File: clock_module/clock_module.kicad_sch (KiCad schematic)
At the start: 19 parts, among them SW1 SW_SPST, SW2 SW_Push, SW3 SW_SPDT, SW4 SW_SPDT, U1 74HC14

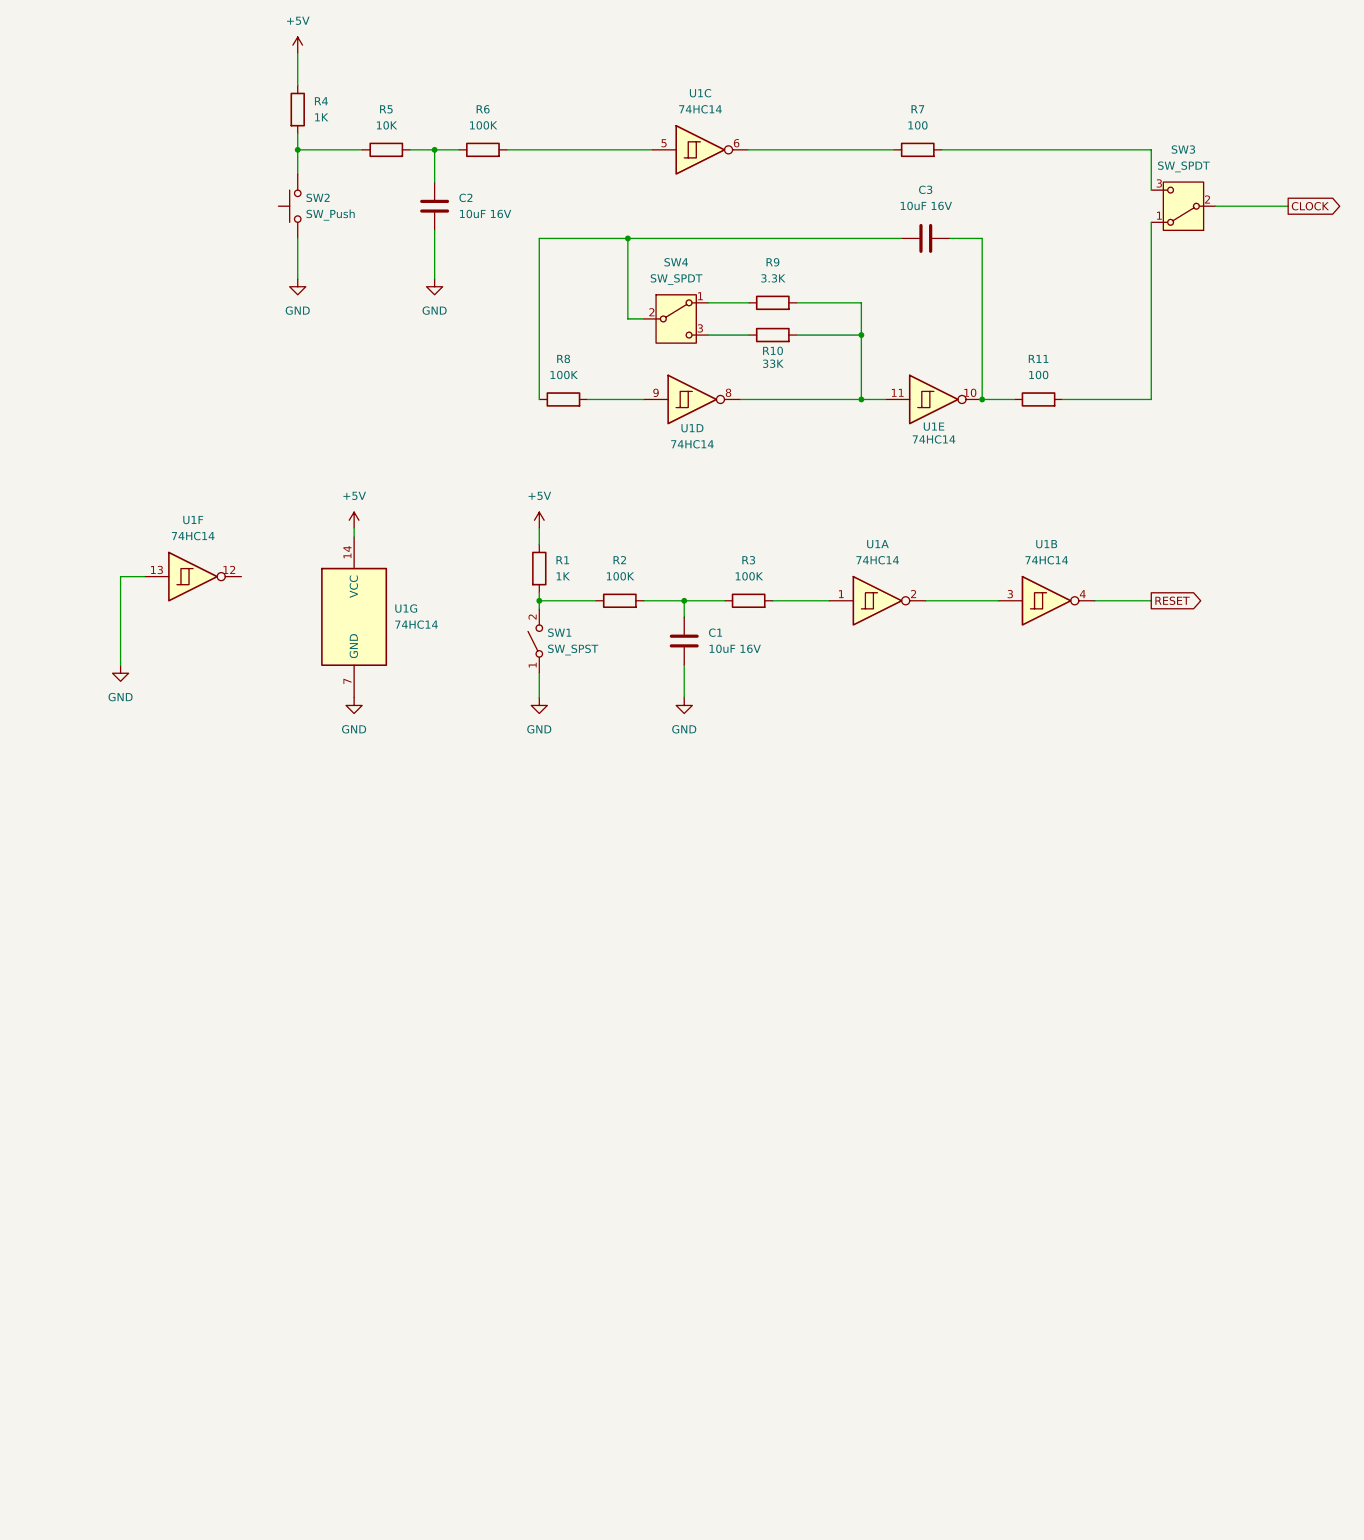
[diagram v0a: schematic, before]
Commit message: フットプリント追加
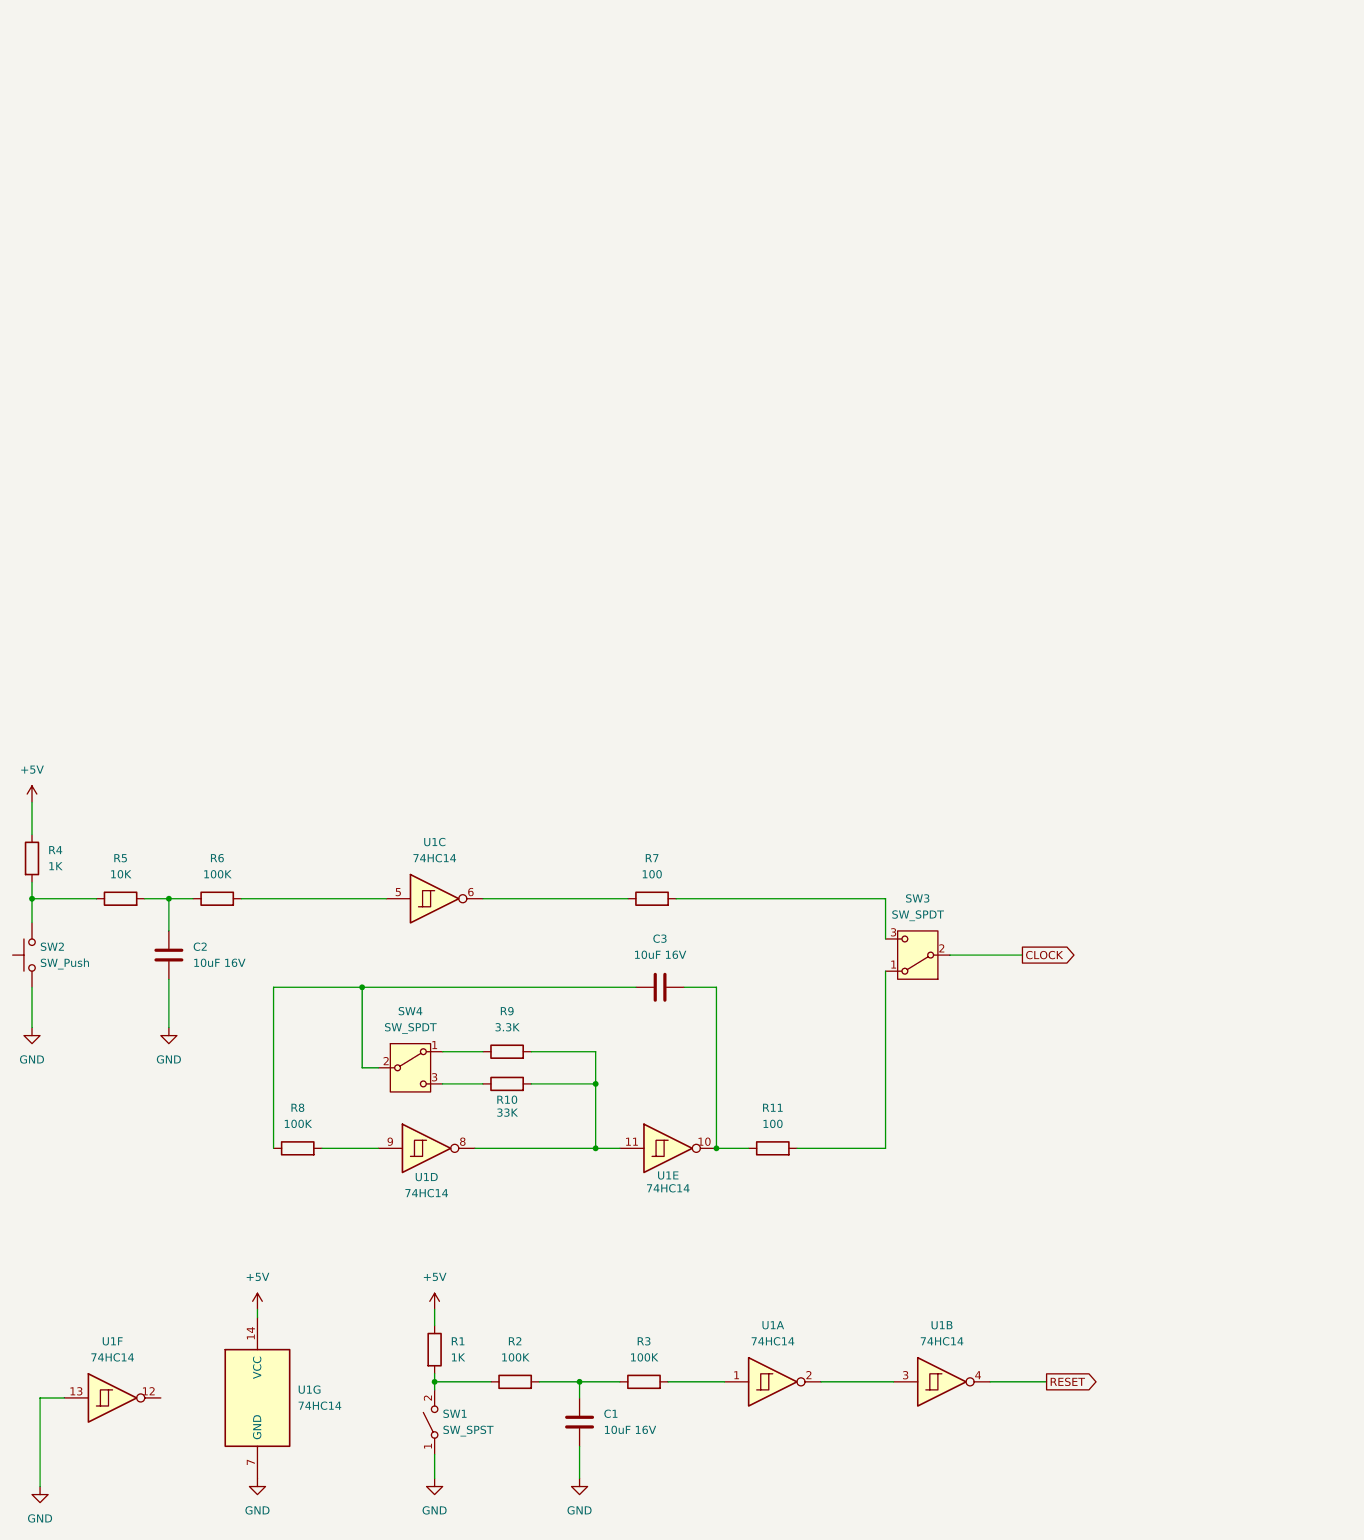
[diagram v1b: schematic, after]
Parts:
- SW3, SW4: footprint footprint_library:SPDT -> footprint_library:SS-12D00G3
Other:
- moved on the sheet: C1, C2, C3, R1, R10, R11, R2, R3, R4, R5, R6, R7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

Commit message: 電源回路wip
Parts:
- added C1: 100uF, Capacitor_THT:C_Disc_D4.3mm_W1.9mm_P5.00mm, symbol Device:C
- added C10, C11, C12, C13, C14, C2, C3, C4, C5, C6, C7, C8, C9: 0.1uF, Capacitor_THT:C_Disc_D4.3mm_W1.9mm_P5.00mm, symbol Device:C
- added J1: USB_C_Receptacle_PowerOnly_6P, footprint_library:UJC-HP-3-SMT-TR, symbol Connector:USB_C_Receptacle_PowerOnly_6P
- added J2: Conn_01x02_Socket, Connector_PinSocket_2.54mm:PinSocket_1x02_P2.54mm_Horizontal, symbol Connector:Conn_01x02_Socket
- added R1: 1K, Resistor_THT:R_Axial_DIN0207_L6.3mm_D2.5mm_P10.16mm_Horizontal, symbol Device:R
- added R2, R3: 5.1K, Resistor_THT:R_Axial_DIN0207_L6.3mm_D2.5mm_P10.16mm_Horizontal, symbol Device:R
- added V1: 5V, symbol Simulation_SPICE:VDC
- renumbered C2 to C15, C3 to C16, C1 to C17, R7 to R10, R1 to R12, R2 to R13, R3 to R14, R8 to R7, R9 to R8, R10 to R9, SW2 to SW1, SW4 to SW2, SW1 to SW4
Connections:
- net +5V: now also C1.1, C10.1, C11.1, C12.1, C13.1, C14.1, C2.1, C3.1, C4.1, C5.1, C6.1, C7.1, C8.1, C9.1, J1.A9 (VBUS), J1.B9 (VBUS), R1.1, V1.1
- net CLOCK: now also J2.1 (Pin_1)
- net GND: now also C1.2, C10.2, C11.2, C12.2, C13.2, C14.2, C2.2, C3.2, C4.2, C5.2, C6.2, C7.2, C8.2, C9.2, J1.A12 (GND), J1.B12 (GND), R1.2, R2.2, R3.2, V1.2
- net RESET: now also J2.2 (Pin_2)
- new net: J1.A5 (CC1), R2.1
- new net: J1.B5 (CC2), R3.1
- no-connect marks 0 -> 2
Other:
- moved on the sheet: C15, C16, C17, R10, R11, R12, R13, R14, R4, R5, R6, R7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

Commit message: 位置調整wip
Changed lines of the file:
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@@
 	(global_label "RESET"
 		(shape output)
-		(at 204.47 237.49 90)
+		(at 204.47 237.49 0)
 		(fields_autoplaced yes)
 		(effects
@@
 		)
 		(property "Intersheetrefs" "${INTERSHEET_REFS}"
-			(at 204.47 228.7597 90)
+			(at 213.2003 237.49 0)
 			(effects
 				(font

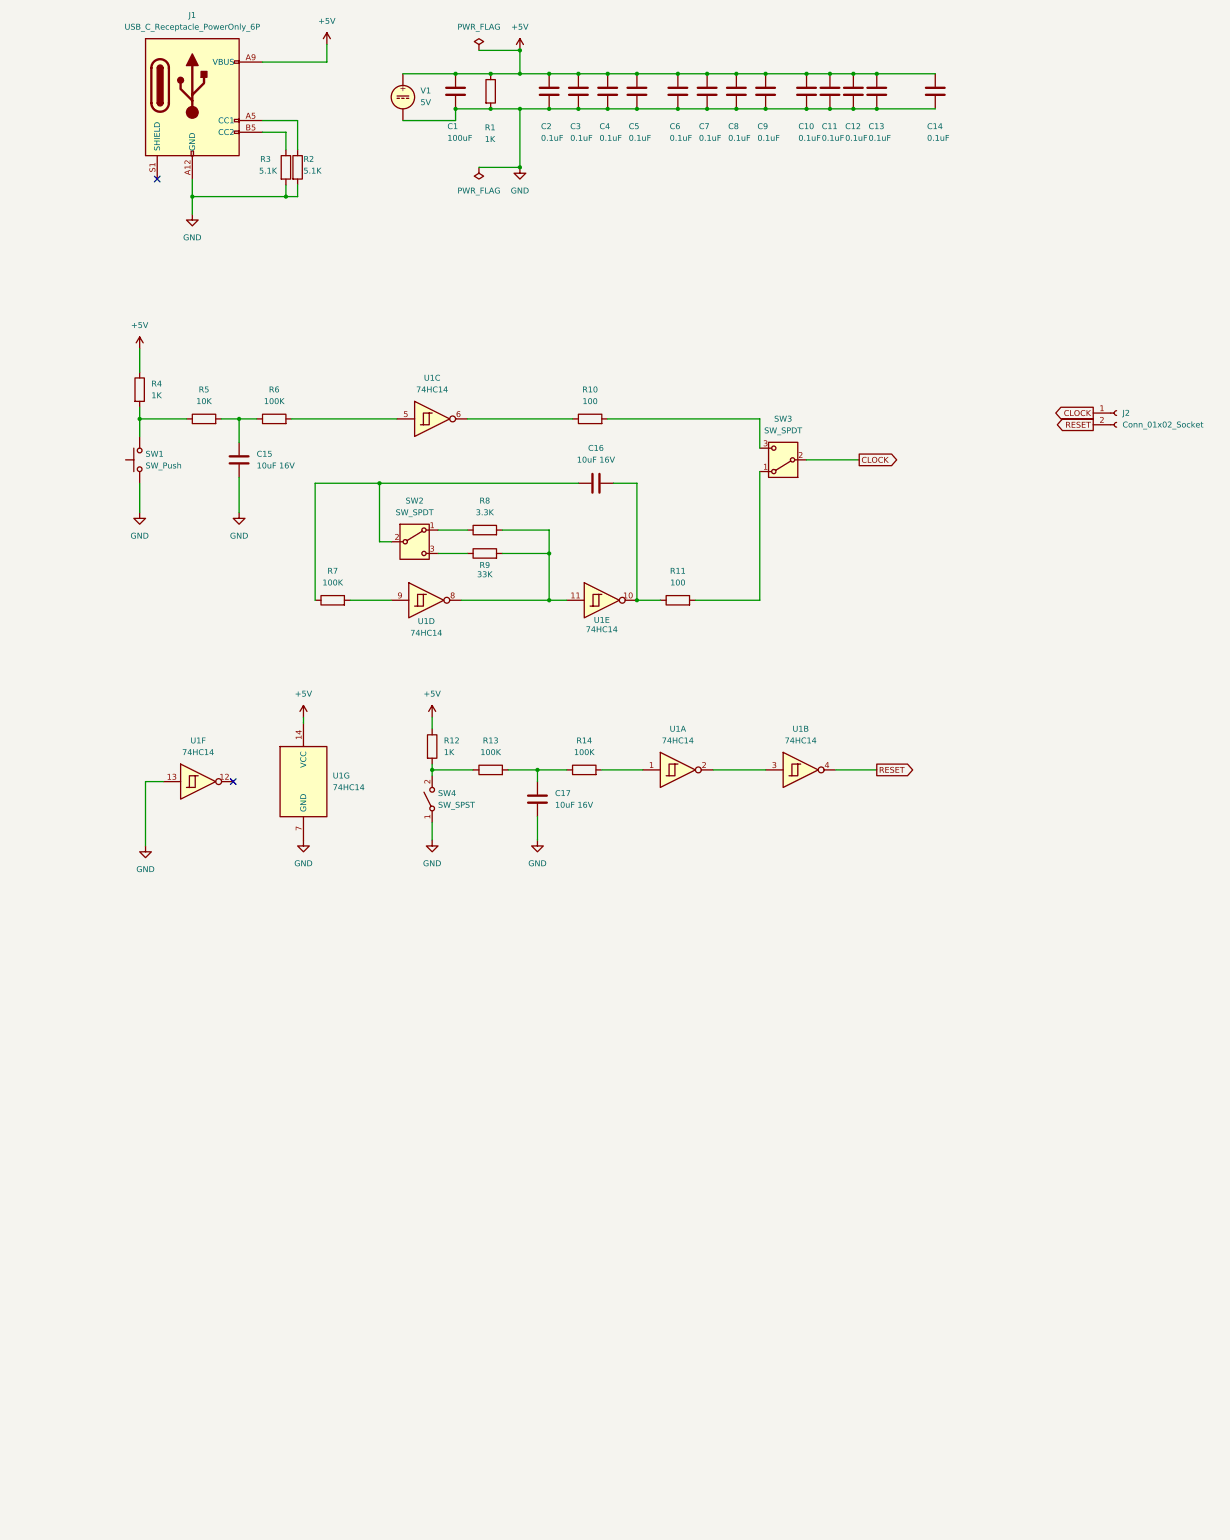
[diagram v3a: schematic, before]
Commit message: クロック、リセット回路の基盤設計
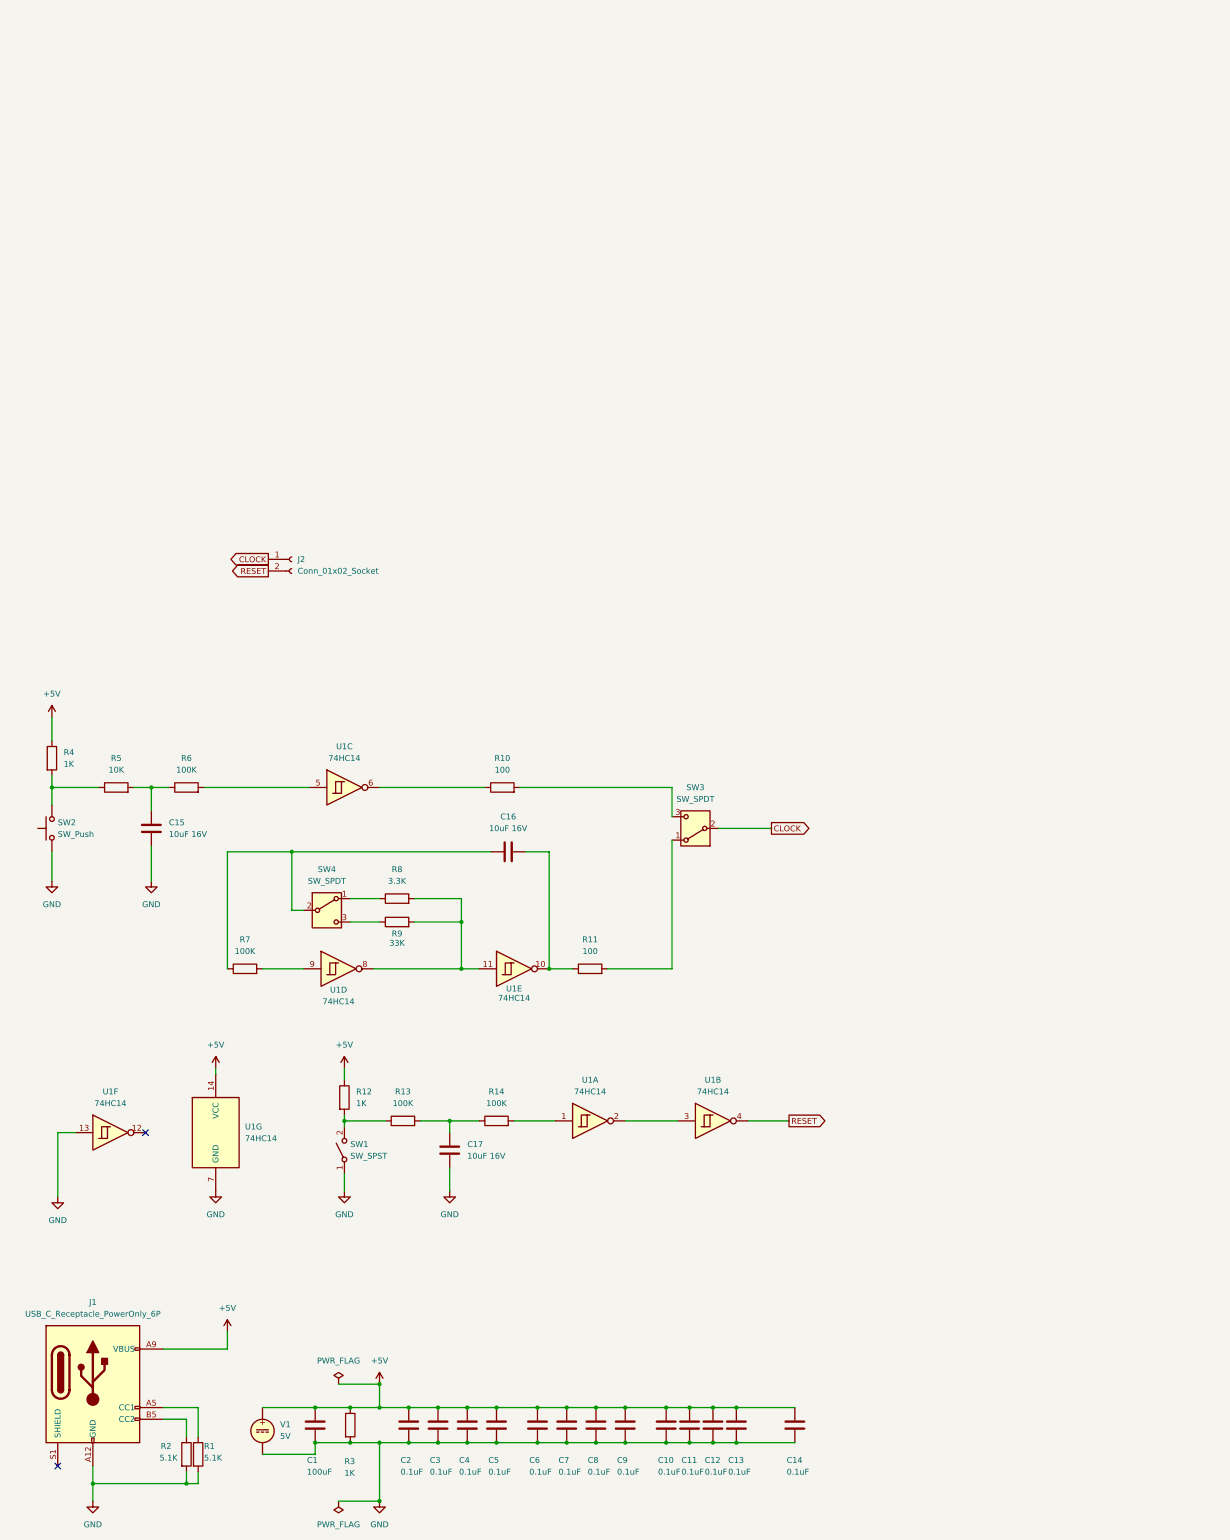
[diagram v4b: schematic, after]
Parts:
- renumbered R2 to R1, R3 to R2, R1 to R3, SW4 to SW1, SW1 to SW2, SW2 to SW4
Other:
- moved on the sheet: C1, C10, C11, C12, C13, C14, C15, C16, C17, C2, C3, C4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

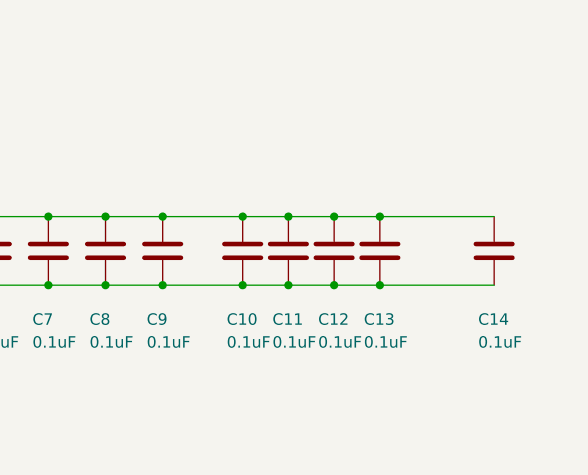
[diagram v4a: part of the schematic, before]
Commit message: 電源位置変更
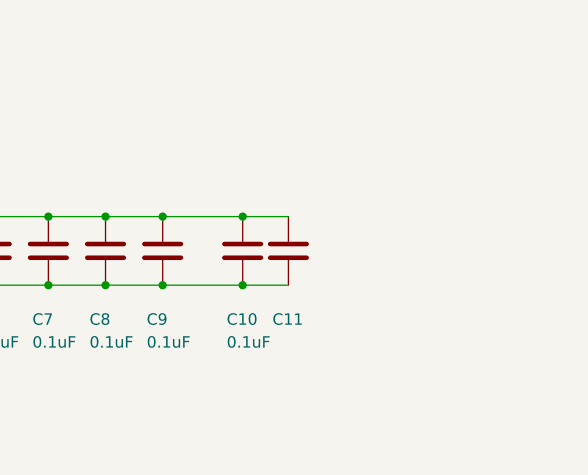
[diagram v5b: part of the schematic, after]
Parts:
- removed C12, C13, C14: 0.1uF, Capacitor_THT:C_Disc_D4.3mm_W1.9mm_P5.00mm, symbol Device:C
- R1, R10, R11, R12, R13, R14, R2, R3, R4, R5, R6, R7, R8, R9: footprint Resistor_THT:R_Axial_DIN0207_L6.3mm_D2.5mm_P10.16mm_Horizontal -> Resistor_THT:R_Axial_DIN0207_L6.3mm_D2.5mm_P2.54mm_Vertical

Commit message: ICをライブラリに追加
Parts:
- removed J2: Conn_01x02_Socket, Connector_PinSocket_2.54mm:PinSocket_1x02_P2.54mm_Horizontal, symbol Connector:Conn_01x02_Socket
- added U2, U3, U4, U5: 74HC161N, footprint_library:74hc161, symbol 74hc161:74HC161N
- added U6, U7: 74HC153N, footprint_library:SOT38-4_NEX, symbol 74hc153:74HC153N
- added U8: CD74HC283E, footprint_library:74hc283, symbol 74hc283:CD74HC283E
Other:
- moved on the sheet: C1, C10, C11, C15, C16, C17, C2, C3, C4, C5, C6, C7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

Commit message: IC追加
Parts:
- added D1, D2, D3, D4: LED, symbol Device:LED
- added R15, R16, R17, R18: R, symbol Device:R
- added U10: 74HC74, symbol 74xx:74HC74
- added U11: SN74HC10N, N14, symbol 74hc10:SN74HC10N
- added U9: SN74HC32N, footprint_library:74hc32, symbol 74hc32:SN74HC32N
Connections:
- net +5V: now also U2.16 (VCC), U3.16 (VCC), U4.16 (VCC), U5.10 (CET), U5.16 (VCC), U5.7 (CEP), U6.16 (VCC), U7.16 (VCC), U8.16 (VCC), U10.14 (VCC), U11.14 (VCC), U9.14 (VCC)
- net CLOCK: now also U2.2 (CP), U3.2 (CP), U4.2 (CP), U5.2 (CP)
- net GND: now also U2.10 (CET), U2.7 (CEP), U2.8 (GND), U3.10 (CET), U3.7 (CEP), U3.8 (GND), U4.10 (CET), U4.7 (CEP), U4.8 (GND), U5.8 (GND), U6.1 (1E*), U6.13 (2I3), U6.15 (2E*), U6.3 (1I3), U6.8 (GND), U7.1 (1E*), U7.13 (2I3), U7.15 (2E*), U7.3 (1I3), U7.8 (GND), U8.8 (GND), D1.1 (K), D2.1 (K), D3.1 (K), D4.1 (K), U10.10 (~{S}), U10.11 (C), U10.12 (D), U10.13 (~{R}), U10.7 (GND), U11.7 (GND), U9.7 (GND)
- net RESET: now also U2.1 (MR*), U3.1 (MR*), U4.1 (MR*), U5.1 (MR*)
- net at U4.11 (Q3): now also R15.2
- net at U4.12 (Q2): now also R16.2
- net at U4.13 (Q1): now also R17.2
- net at U4.14 (Q0): now also R18.2
- net at U4.3 (D0): now also U2.3 (D0), U3.3 (D0), U5.3 (D0), U8.4 (S0)
- net at U4.4 (D1): now also U2.4 (D1), U3.4 (D1), U5.4 (D1), U8.1 (S1)
- net at U4.5 (D2): now also U2.5 (D2), U3.5 (D2), U5.5 (D2), U8.13 (S2)
- net at U4.6 (D3): now also U2.6 (D3), U3.6 (D3), U5.6 (D3), U8.10 (S3)
- net at U7.10 (2I0): now also U2.11 (Q3)
- net at U7.11 (2I1): now also U3.11 (Q3)
- net at U7.5 (1I1): now also U3.12 (Q2)
- net at U7.6 (1I0): now also U2.12 (Q2)
- net at U7.7 (1Y): now also U8.14 (A2)
- net at U7.9 (2Y): now also U8.12 (A3)
- net at U6.10 (2I0): now also U2.13 (Q1)
- net at U6.11 (2I1): now also U3.13 (Q1)
- net at U6.5 (1I1): now also U3.14 (Q0)
- net at U6.6 (1I0): now also U2.14 (Q0)
- net at U6.7 (1Y): now also U8.5 (A0)
- net at U6.9 (2Y): now also U8.3 (A1)
- net A3: now reaches U5.11 (Q3)
- net A2: now reaches U5.12 (Q2)
- net A1: now reaches U5.13 (Q1)
- net A0: now reaches U5.14 (Q0)
- new net: D1.2 (A), R15.1
- new net: D2.2 (A), R16.1
- new net: D3.2 (A), R17.1
- new net: D4.2 (A), R18.1
- no-connect marks 2 -> 8
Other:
- moved on the sheet: U2, U3, U4, U5, U6, U7, U8
